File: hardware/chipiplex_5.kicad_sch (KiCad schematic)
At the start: 30 parts, among them Q10 MMBT3906, Q11 MMBT3906, Q12 MMBT3906, Q17 MMBT3906, Q9 MMBT3906

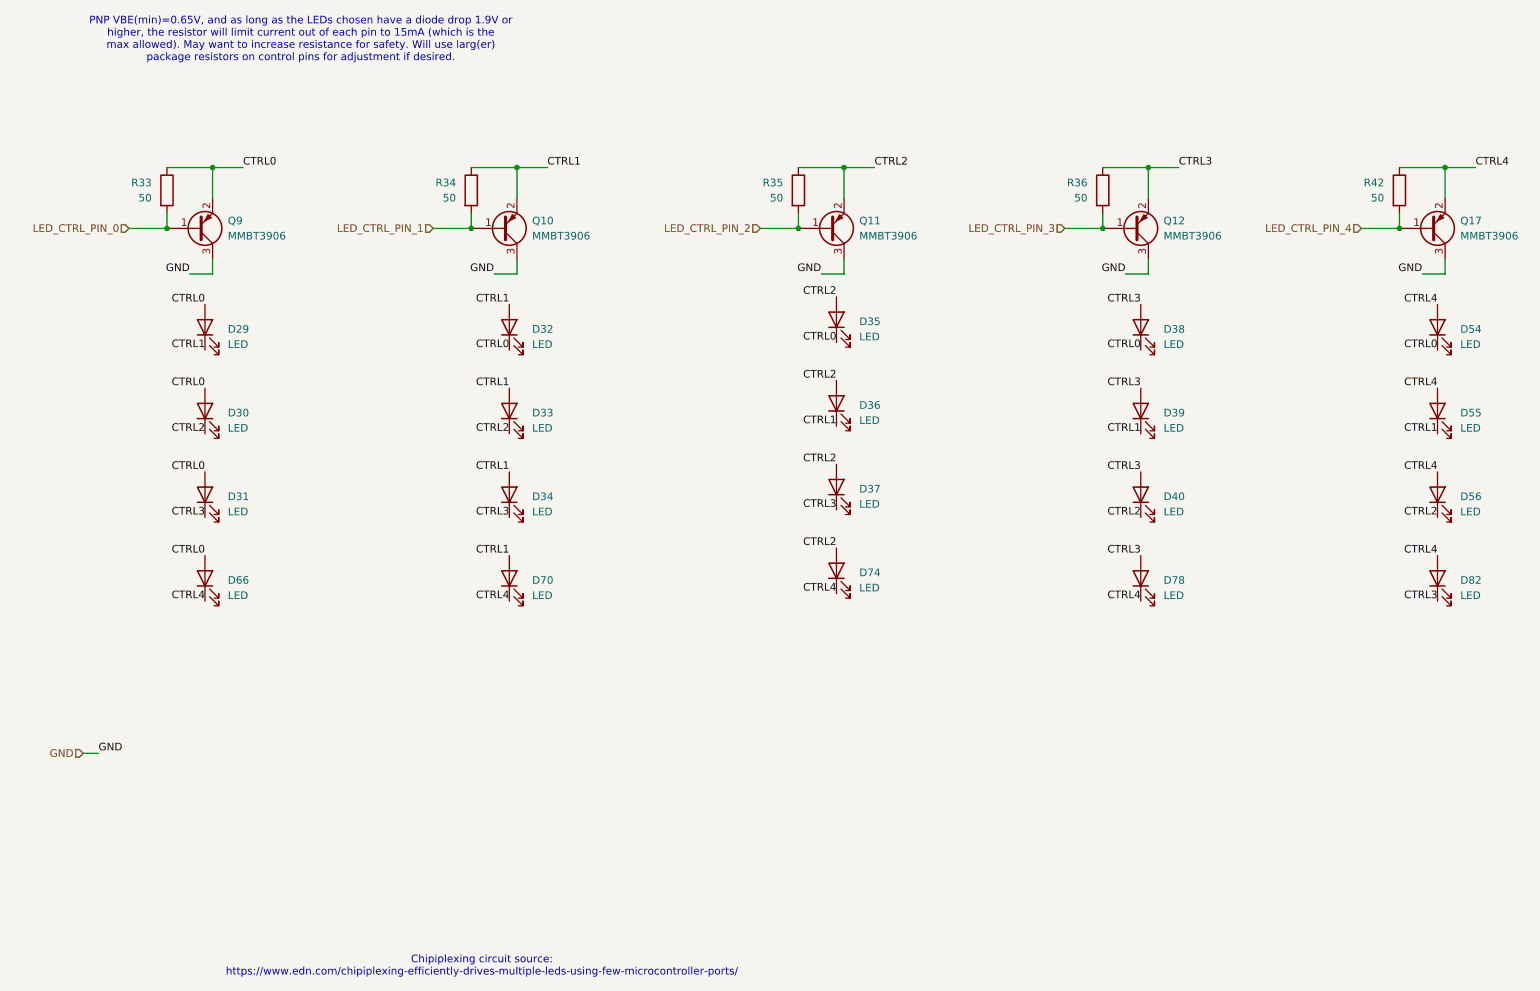
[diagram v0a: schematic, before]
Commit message: [Hardware] Replace LISDH Motion Sensor with LSM6DSM
Change motion sensor to an accelerometer + gyro unit. Route the second interrupt line to the STM32.
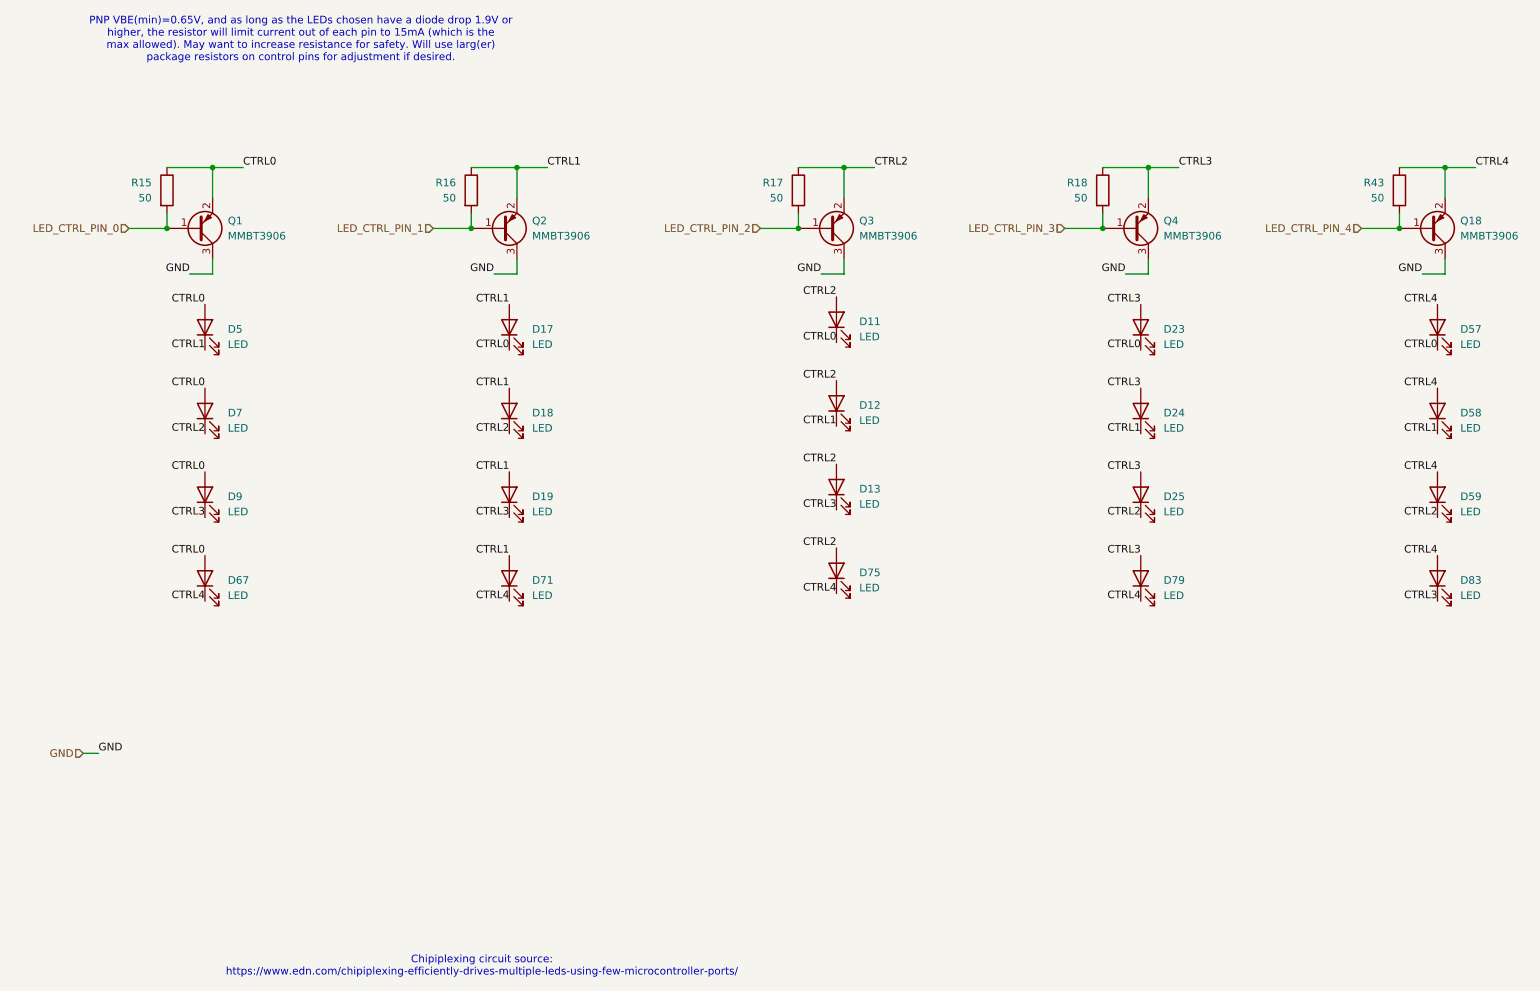
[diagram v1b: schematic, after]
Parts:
- renumbered D35 to D11, D36 to D12, D37 to D13, D32 to D17, D33 to D18, D34 to D19, D38 to D23, D39 to D24, D40 to D25, D29 to D5, D54 to D57, D55 to D58, D56 to D59, D66 to D67, D30 to D7, D70 to D71, D74 to D75, D78 to D79, D82 to D83, D31 to D9, Q9 to Q1, Q17 to Q18, Q10 to Q2, Q11 to Q3, Q12 to Q4, R33 to R15, R34 to R16, R35 to R17, R36 to R18, R42 to R43

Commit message: Change many passives to 0402 and assign part numbers
Incorporate 0402 parts where possible
Assign Manufacturer Part Numbers to parts where possible
Update layout for the new passive sizes
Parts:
- D11, D12, D13, D17, D18, D19, D23, D24, D25, D5, D57, D58, D59, D67, D7, D71, D75, D79, D83, D9: MPN (none) -> LTST-C171GKT
- Q1, Q18, Q2, Q3, Q4: MPN (none) -> MMBT3906
- R15, R16, R17, R18, R43: footprint Resistor_SMD:R_0603_1608Metric_Pad0.98x0.95mm_HandSolder -> Resistor_SMD:R_0402_1005Metric; MPN (none) -> RC0402JR-0750RL
